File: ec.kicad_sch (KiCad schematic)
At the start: 50 parts, among them IC1 ADM3260ARSZ-RL7, J1 EC, J2 Temp, U2 ADS1115IDGS, U4 TPS60400DBV, U5 LM324, U6 MCP4017T-502E/LT

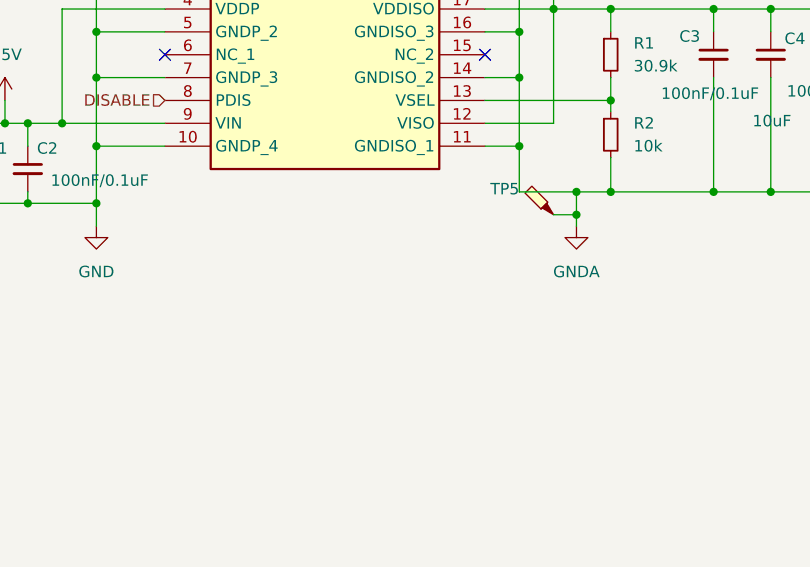
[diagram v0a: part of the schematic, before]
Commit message: Fix ERC warnings
See #28
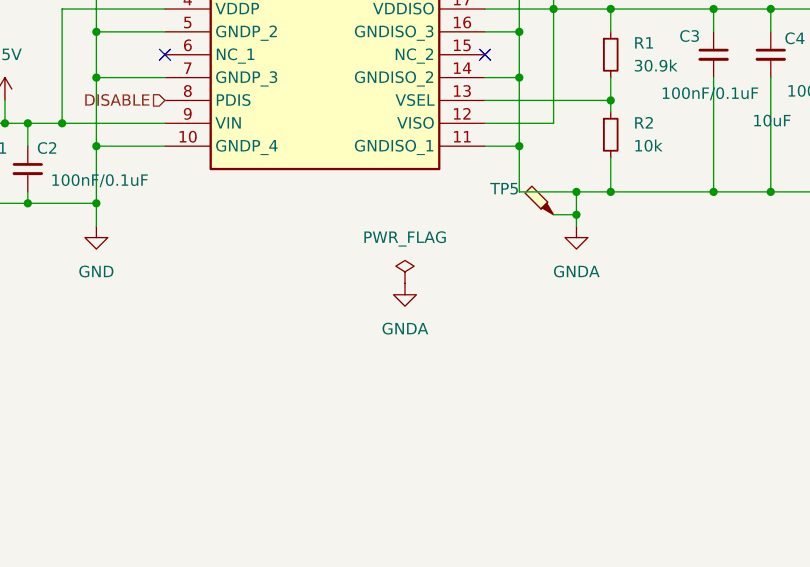
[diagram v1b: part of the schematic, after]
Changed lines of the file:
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@@
+	)
+	(symbol
+		(lib_id "power:PWR_FLAG")
+		(at 67.31 146.05 0)
+		(unit 1)
+		(exclude_from_sim no)
+		(in_bom yes)
+		(on_board yes)
+		(dnp no)
+		(fields_autoplaced yes)
+		(property "Reference" "#FLG06"
+			(at 67.31 144.145 0)
+			(effects
+				(font
+					(size 1.27 1.27)
+				)
+				(hide yes)
+			)
+		)
+		(property "Value" "PWR_FLAG"
+			(at 67.31 140.97 0)
+			(effects
+				(font
+					(size 1.27 1.27)
+				)
+			)
+		)
+		(property "Footprint" ""
+			(at 67.31 146.05 0)
+			(effects
+				(font
+					(size 1.27 1.27)
+				)
+				(hide yes)
+			)
+		)
+		(property "Datasheet" "~"
+			(at 67.31 146.05 0)
+			(effects
+				(font
+					(size 1.27 1.27)
+				)
+				(hide yes)
+			)
+		)
+		(property "Description" "Special symbol for telling ERC where power comes from"
+			(at 67.31 146.05 0)
+			(effects
+				(font
+					(size 1.27 1.27)
+				)
+				(hide yes)
+			)
+		)
+		(pin "1"
+		)
+		(instances
+			(project "HydroponicFlowerControl"
+				(path "/b3c8a28b-9ce1-4002-b8e8-ef8cb73fe031/2418e7ae-ca6e-4e69-b6d2-7ffd3e4dd695"
+					(reference "#FLG06")
+					(unit 1)
+				)
+			)
+		)
 	)
 	(symbol
@@
 					(unit 1)
 				)
+			)
+		)
+	)
+	(symbol
+		(lib_id "power:GNDA")
+		(at 67.31 146.05 0)
+		(unit 1)
+		(exclude_from_sim no)
+		(in_bom yes)
+		(on_board yes)
+		(dnp no)
+		(fields_autoplaced yes)
+		(property "Reference" "#PWR0114"
+			(at 67.31 152.4 0)
+			(effects
+				(font
+					(size 1.27 1.27)
+				)
+				(hide yes)
+			)
+		)
+		(property "Value" "GNDA"
+			(at 67.31 151.13 0)
+			(effects
+				(font
+					(size 1.27 1.27)
+				)
+			)
+		)
+		(property "Footprint" ""
+			(at 67.31 146.05 0)
+			(effects
+				(font
+					(size 1.27 1.27)
+				)
+				(hide yes)
+			)
+		)
+		(property "Datasheet" ""
+			(at 67.31 146.05 0)
+			(effects
+				(font
+					(size 1.27 1.27)
+				)
+				(hide yes)
+			)
+		)
+		(property "Description" "Power symbol creates a global label with name \"GNDA\" , analog ground"
+			(at 67.31 146.05 0)
+			(effects
+				(font
+					(size 1.27 1.27)
+				)
+				(hide yes)
+			)
+		)
+		(pin "1"
+		)
+		(instances
+			(project "HydroponicFlowerControl"
+				(path "/b3c8a28b-9ce1-4002-b8e8-ef8cb73fe031/2418e7ae-ca6e-4e69-b6d2-7ffd3e4dd695"
+					(reference "#PWR0114")
+					(unit 1)
+				)

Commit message: Update part for JST 2P connectors
Closes #41
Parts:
- J1, J2: LCSC C493111 -> C157931
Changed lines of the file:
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@@
 			)
 		)
-		(property "LCSC" "C493111"
+		(property "LCSC" "C157931"
 			(at 163.83 35.56 0)
 			(effects
@@
 			)
 		)
-		(property "LCSC" "C493111"
+		(property "LCSC" "C157931"
 			(at 198.12 102.87 0)
 			(effects

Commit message: Update manufacturing positions and rotations of parts
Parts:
- J1, J2: JLCPCB Position Offset (none) -> 0,3.5; JLCPCB Rotation Offset (none) -> 180
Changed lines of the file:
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@@
 			)
 		)
+		(property "JLCPCB Position Offset" "0,3.5"
+			(at 163.83 35.56 0)
+			(effects
+				(font
+					(size 1.27 1.27)
+				)
+				(hide yes)
+			)
+		)
+		(property "JLCPCB Rotation Offset" "180"
+			(at 163.83 35.56 0)
+			(effects
+				(font
+					(size 1.27 1.27)
+				)
+				(hide yes)
+			)
+		)
 		(pin "1"
 		)
@@
 			(at 198.12 102.87 0)
 			(effects
+				(font
+					(size 1.27 1.27)
+				)
+				(hide yes)
+			)
+		)
+		(property "JLCPCB Rotation Offset" "180"
+			(at 198.12 102.87 0)
+			(effects
+				(font
+					(size 1.27 1.27)
+				)
+				(hide yes)
+			)
+		)
+		(property "JLCPCB Position Offset" "0,3.5"
+			(at 198.12 102.87 0)
+			(effects

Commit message: Include THT components in manufacturing
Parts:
- J1, J2: now in the parts list
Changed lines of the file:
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@@
 		(unit 1)
 		(exclude_from_sim no)
-		(in_bom no)
+		(in_bom yes)
 		(on_board yes)
 		(dnp no)
@@
 		(unit 1)
 		(exclude_from_sim no)
-		(in_bom no)
+		(in_bom yes)
 		(on_board yes)
 		(dnp no)
